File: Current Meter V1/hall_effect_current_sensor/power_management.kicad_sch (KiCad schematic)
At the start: 20 parts, among them J1 USB_C_Receptacle_PowerOnly_6P, SW1 SW_DIP_x01, U2 TPS5430DDAR

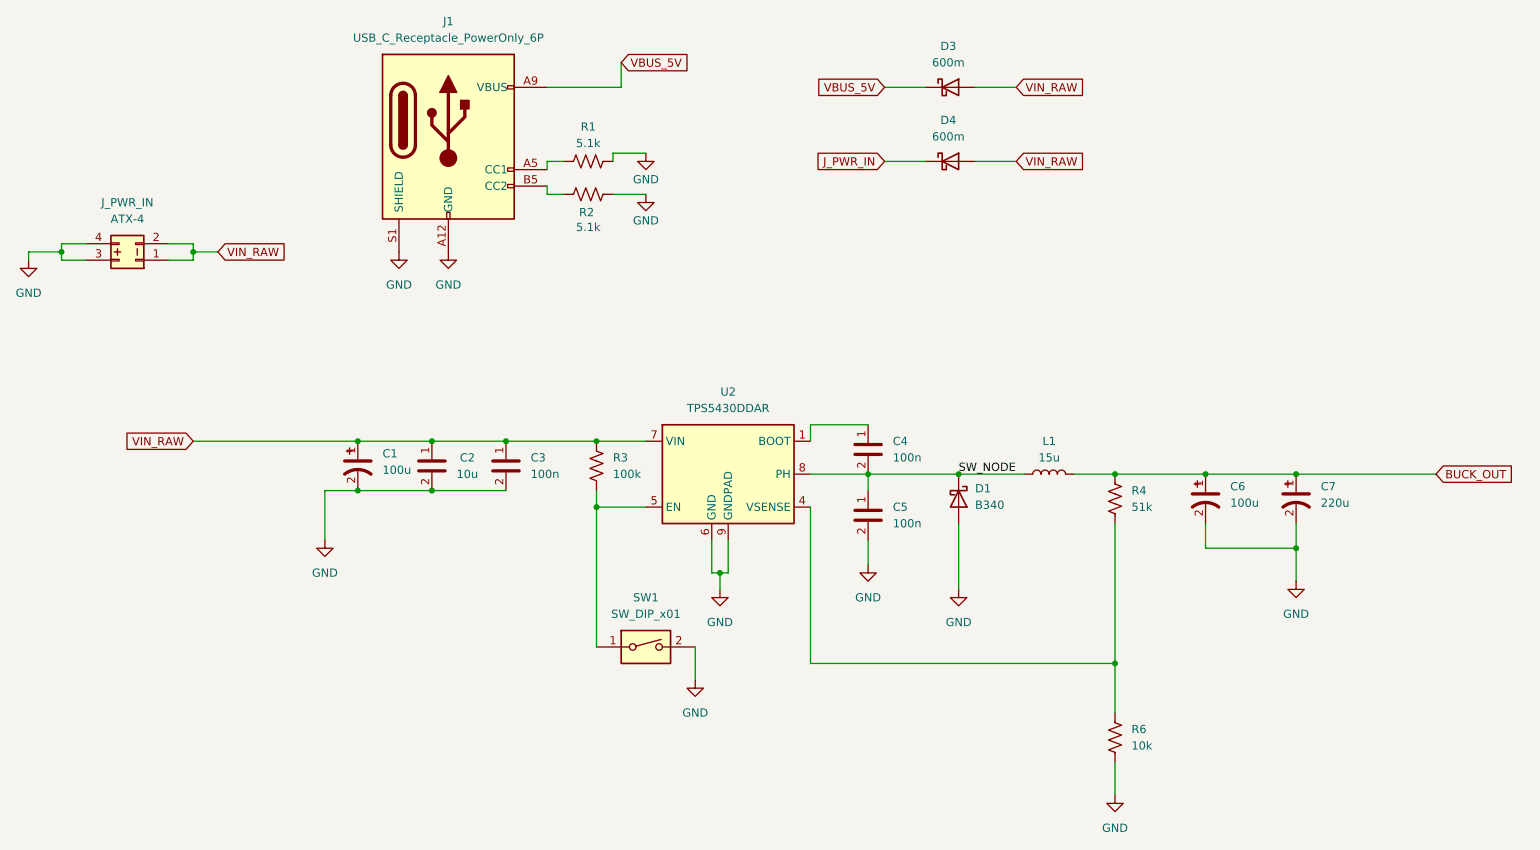
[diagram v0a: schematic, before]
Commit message: buck_converter
addition of power management
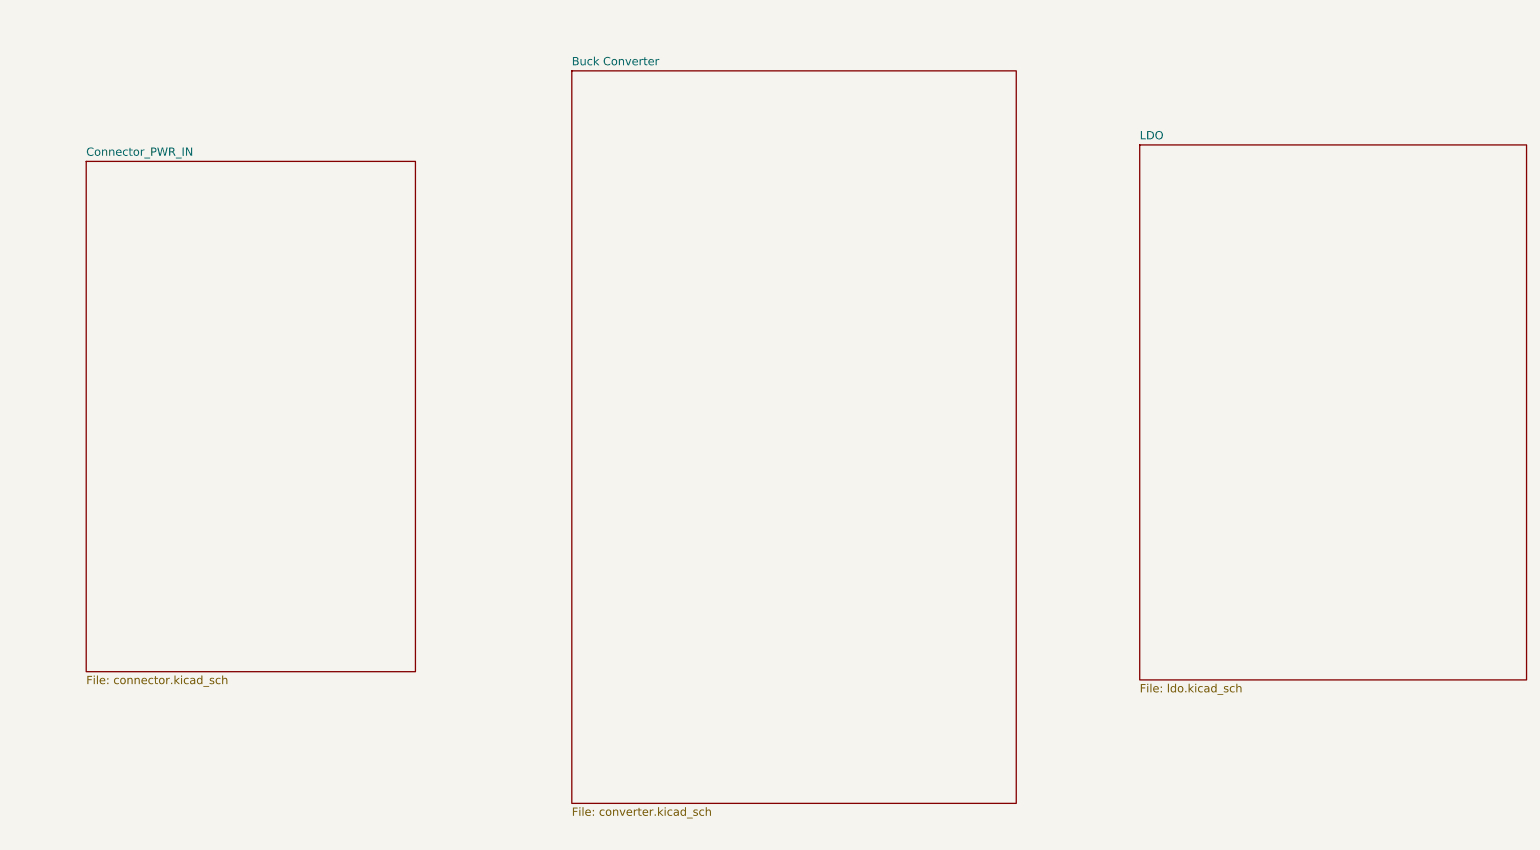
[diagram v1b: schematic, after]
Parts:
- removed C1, C6: 100u, Capacitor_THT:CP_Radial_D8.0mm_P3.50mm, symbol bfr_capacitors:50ZLH100MEFC8X11.5
- removed C2: 10u, Capacitor_SMD:C_0603_1608Metric, symbol bfr_capacitors:CL05A106MQ5NUNC
- removed C3, C4, C5: 100n, Capacitor_SMD:C_0402_1005Metric_Pad0.74x0.62mm_HandSolder, symbol bfr_capacitors:CL05B104KB54PNC
- removed C7: 220u, Capacitor_THT:CP_Radial_D8.0mm_P3.50mm, symbol bfr_capacitors:35ZLH220MEFC8X11.5
- removed D1: B340, Diode_SMD:D_SMC, symbol Diode:B340
- removed D3, D4: 600m, Diode_SMD:D_SOD-323_HandSoldering, symbol bfr_diodes:1N5819WS
- removed J1: USB_C_Receptacle_PowerOnly_6P, symbol Connector:USB_C_Receptacle_PowerOnly_6P
- removed J_PWR_IN: ATX-4, Connector_Molex:Molex_Mini-Fit_Jr_5566-04A_2x02_P4.20mm_Vertical, symbol bfr_connectors:ATX-4
- removed L1: 15u, Inductor_SMD:L_6.3x6.3_H3, symbol bfr_inductors:CDRH104RNP-150NC
- removed R1, R2: 5.1k, Resistor_SMD:R_0402_1005Metric_Pad0.72x0.64mm_HandSolder, symbol bfr_resistors:RMCF0402FT5K10
- removed R3: 100k, Resistor_SMD:R_0402_1005Metric_Pad0.72x0.64mm_HandSolder, symbol bfr_resistors:RMCF0402FT100K
- removed R4: 51k, Resistor_SMD:R_0402_1005Metric_Pad0.72x0.64mm_HandSolder, symbol bfr_resistors:RMCF0402FT51K0
- removed R6: 10k, Resistor_SMD:R_0402_1005Metric_Pad0.72x0.64mm_HandSolder, symbol bfr_resistors:RMCF0402FT10K0
- removed SW1: SW_DIP_x01, Button_Switch_SMD:SW_DIP_SPSTx01_Slide_6.7x4.1mm_W6.73mm_P2.54mm_LowProfile_JPin, symbol Switch:SW_DIP_x01
- removed U2: TPS5430DDAR, Package_SO:TI_SO-PowerPAD-8_ThermalVias, symbol bfr_power_ics:TPS5430DDAR
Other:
- added sheet Buck Converter (converter.kicad_sch)
- added sheet Connector_PWR_IN (connector.kicad_sch)
- added sheet LDO (ldo.kicad_sch)
